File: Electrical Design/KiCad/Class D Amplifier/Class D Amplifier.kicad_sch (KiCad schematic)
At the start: 26 parts, among them J1 AudioJack3, J2 speakON_NL2MDXX-V, J3 Barrel_Jack, U1 TPA3136D2PWPR

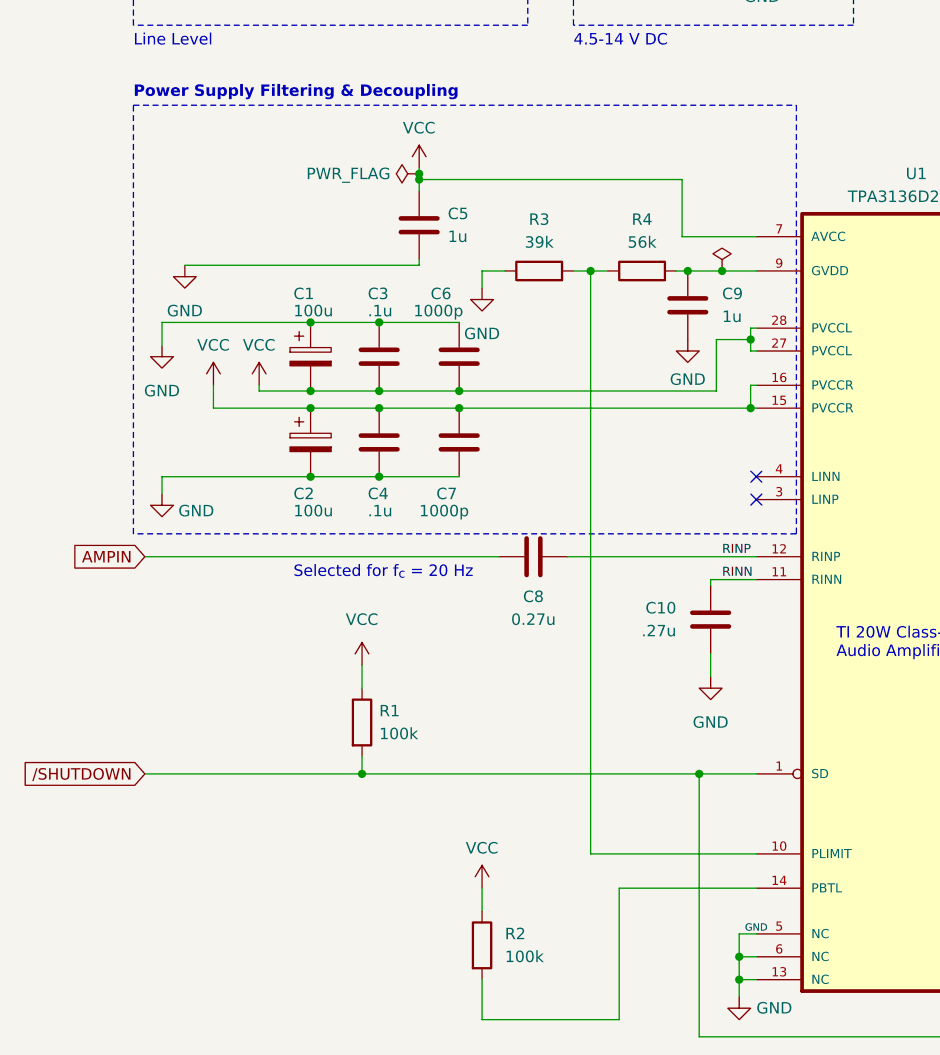
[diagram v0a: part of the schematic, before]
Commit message: add PDS, modified amp footprint, organizational changes
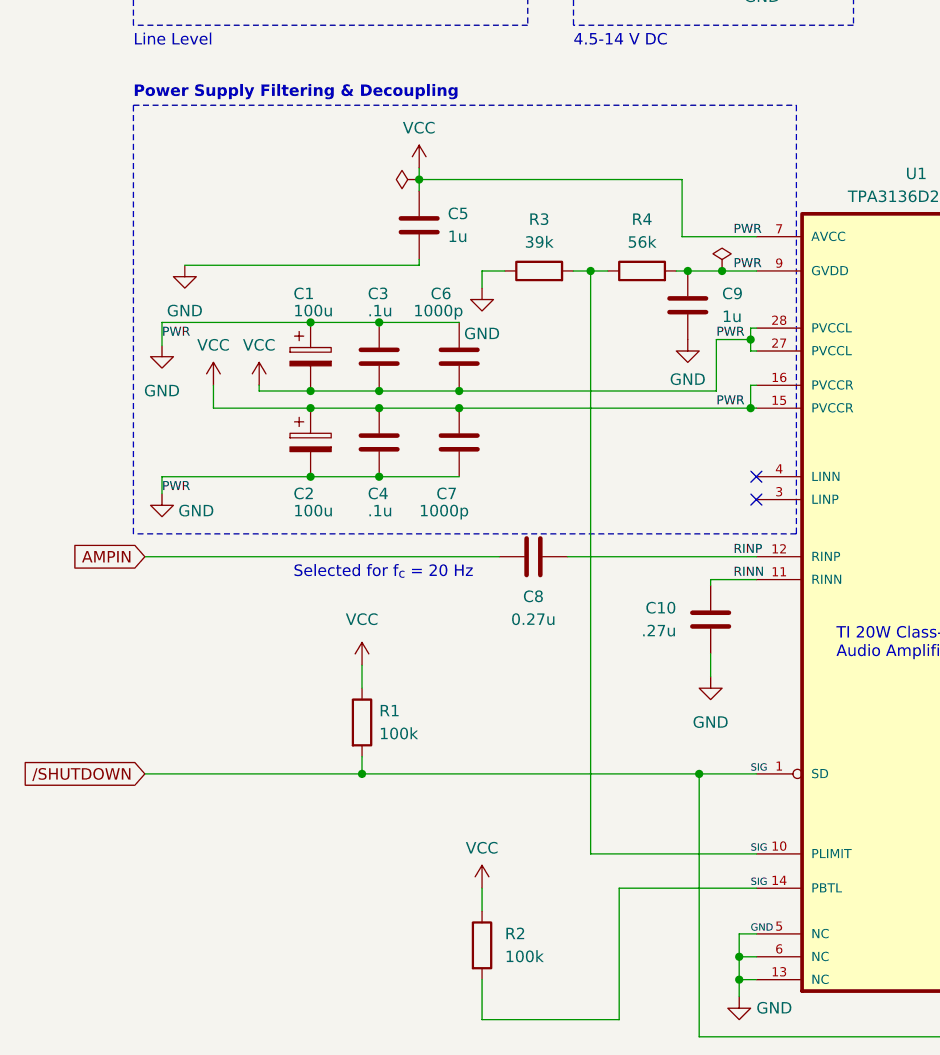
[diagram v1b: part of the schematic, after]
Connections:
- net VCC is gone; now on net GND: C1.2, C2.1, C3.2, C4.1, C5.1, C6.2, C7.1, J3.1, R1.1, R2.1, U1.15 (PVCCR), U1.16 (PVCCR), U1.27 (PVCCL), U1.28 (PVCCL), U1.7 (AVCC)
- net GND: now also C9.2, R4.2, U1.9 (GVDD)
- net /SHUTDOWN: now also R2.2, R3.2, R4.1, U1.10 (PLIMIT), U1.14 (PBTL)
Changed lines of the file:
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@@
   (junction (at 136.525 88.9) (diameter 0) (color 0 0 0 0)
-  )
-  (junction (at 99.695 62.865) (diameter 0) (color 0 0 0 0)
   )
   (junction (at 212.09 104.14) (diameter 0) (color 0 0 0 0)
@@
     (stroke (width 0) (type default))
   )
-  (wire (pts (xy 99.695 62.865) (xy 99.695 63.5))
+  (wire (pts (xy 99.695 62.23) (xy 99.695 63.5))
     (stroke (width 0) (type default))
   )
@@
   )
   (wire (pts (xy 95.25 88.9) (xy 104.14 88.9))
-    (stroke (width 0) (type default))
-  )
-  (wire (pts (xy 99.695 62.23) (xy 99.695 62.865))
     (stroke (width 0) (type default))
   )
@@
     (effects (font (size 1.27 1.27)) (justify left bottom))
   )
+  (label "PWR" (at 71.12 98.425 0) (fields_autoplaced)
+    (effects (font (size 1 1)) (justify left bottom))
+  )
   (label "SPKR" (at 203.835 85.09 0) (fields_autoplaced)
     (effects (font (size 1.27 1.27)) (justify left bottom))
   )
+  (label "SIG" (at 136.525 129.54 0) (fields_autoplaced)
+    (effects (font (size 0.8 0.8)) (justify left bottom))
+  )
   (label "GND" (at 173.355 143.51 0) (fields_autoplaced)
     (effects (font (size 0.8 0.8)) (justify left bottom))
   )
-  (label "RINP" (at 133.35 105.41 0) (fields_autoplaced)
+  (label "RINP" (at 134.62 105.41 0) (fields_autoplaced)
     (effects (font (size 1 1)) (justify left bottom))
   )
@@
     (effects (font (size 0.6 0.6)) (justify left bottom))
   )
+  (label "PWR" (at 132.715 88.9 0) (fields_autoplaced)
+    (effects (font (size 1 1)) (justify left bottom))
+  )
   (label "OFILTER" (at 175.895 97.79 0) (fields_autoplaced)
     (effects (font (size 0.6 0.6)) (justify left bottom))
   )
-  (label "GND" (at 135.89 147.32 0) (fields_autoplaced)
+  (label "SIG" (at 136.525 138.43 0) (fields_autoplaced)
     (effects (font (size 0.8 0.8)) (justify left bottom))
+  )
+  (label "GND" (at 136.525 147.32 0) (fields_autoplaced)
+    (effects (font (size 0.8 0.8)) (justify left bottom))
+  )
+  (label "PWR" (at 134.62 69.85 0) (fields_autoplaced)
+    (effects (font (size 1 1)) (justify left bottom))
   )
   (label "SPKR" (at 203.835 104.14 0) (fields_autoplaced)
     (effects (font (size 1.27 1.27)) (justify left bottom))
   )
-  (label "RINN" (at 133.35 107.95 0) (fields_autoplaced)
+  (label "PWR" (at 71.12 81.28 0) (fields_autoplaced)
+    (effects (font (size 1 1)) (justify left bottom))
+  )
+  (label "PWR" (at 132.715 81.28 0) (fields_autoplaced)
+    (effects (font (size 1 1)) (justify left bottom))
+  )
+  (label "SIG" (at 136.525 142.24 0) (fields_autoplaced)
+    (effects (font (size 0.8 0.8)) (justify left bottom))
+  )
+  (label "RINN" (at 134.62 107.95 0) (fields_autoplaced)
+    (effects (font (size 1 1)) (justify left bottom))
+  )
+  (label "PWR" (at 134.62 73.66 0) (fields_autoplaced)
     (effects (font (size 1 1)) (justify left bottom))
   )
@@
     )
   )
-  (symbol (lib_id "power:PWR_FLAG") (at 99.695 62.865 90) (unit 1)
-    (in_bom yes) (on_board yes) (dnp no) (fields_autoplaced)
-    (property "Reference" "#FLG02" (at 97.79 62.865 0)
-      (effects (font (size 1.27 1.27)) hide)
-    )
-    (property "Value" "PWR_FLAG" (at 96.52 62.865 90)
-      (effects (font (size 1.27 1.27)) (justify left))
-    )
-    (property "Footprint" "" (at 99.695 62.865 0)
-      (effects (font (size 1.27 1.27)) hide)
-    )
-    (property "Datasheet" "~" (at 99.695 62.865 0)
-      (effects (font (size 1.27 1.27)) hide)
-    )
+  (symbol (lib_id "power:PWR_FLAG") (at 99.695 63.5 90) (unit 1)
+    (in_bom yes) (on_board yes) (dnp no) (fields_autoplaced)
+    (property "Reference" "#FLG02" (at 97.79 63.5 0)
+      (effects (font (size 1.27 1.27)) hide)
+    )
+    (property "Value" "PWR_FLAG" (at 96.52 63.5 90)
+      (effects (font (size 1.27 1.27)) (justify left) hide)
+    )
+    (property "Footprint" "" (at 99.695 63.5 0)
+      (effects (font (size 1.27 1.27)) hide)
+    )
+    (property "Datasheet" "~" (at 99.695 63.5 0)
+      (effects (font (size 1.27 1.27)) hide)
+    )
